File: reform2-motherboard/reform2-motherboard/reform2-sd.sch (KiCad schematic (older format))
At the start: 4 parts, among them J3 SD_Card

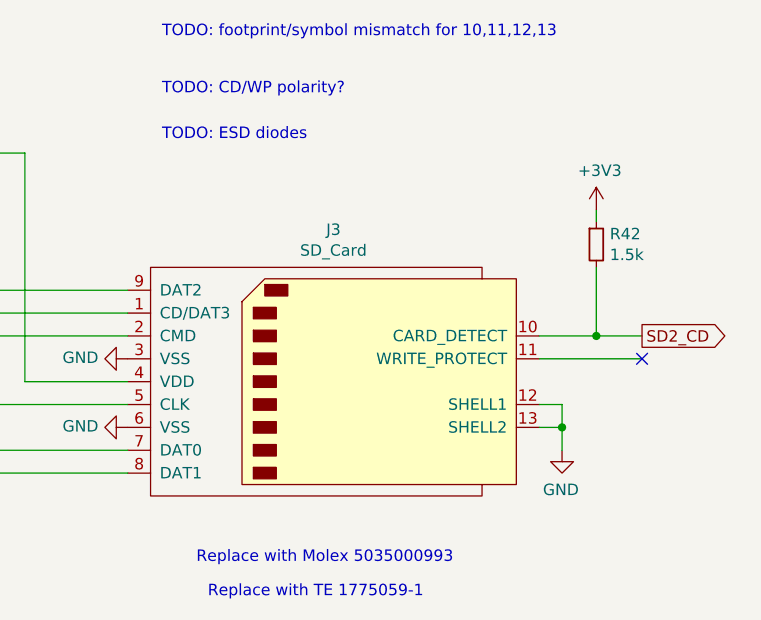
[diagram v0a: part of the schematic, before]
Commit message: reform2 motherboard: pinout and footprint checks completed; ERC checks fixed 100%
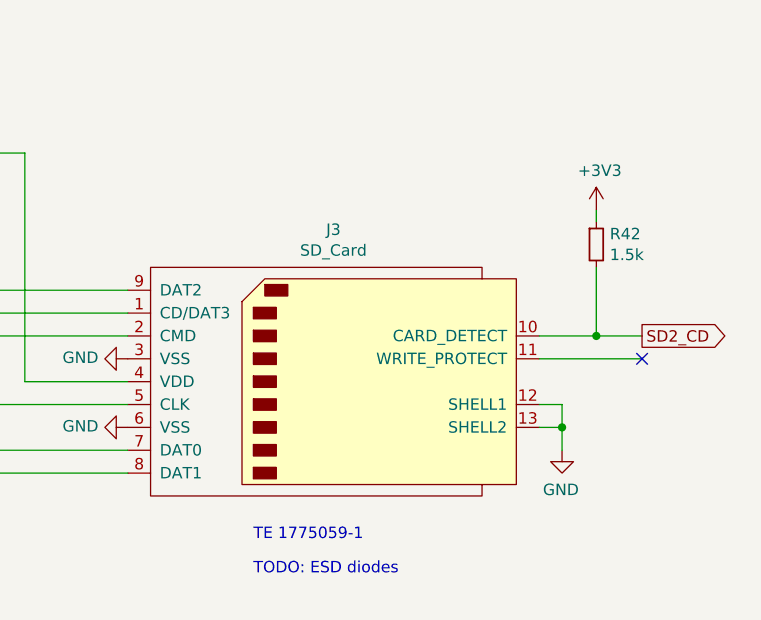
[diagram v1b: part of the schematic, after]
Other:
- note added: "TE 1775059-1"
- note removed: "Replace with Molex 5035000993"
- note removed: "Replace with TE 1775059-1"
- note removed: "TODO: CD/WP polarity?"
- note removed: "TODO: footprint/symbol mismatch for 10,11,12,13"
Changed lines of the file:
@@
 F 1 "SD_Card" H 6200 4024 50  0000 C CNN
 F 2 "footprints:TE_1775059-1" H 6200 3450 50  0001 C CNN
-F 3 "http://portal.fciconnect.com/Comergent//fci/drawing/10067847.pdf" H 6200 3450 50  0001 C CNN
+F 3 "https://www.te.com/usa-en/product-1775059-1.html" H 6200 3450 50  0001 C CNN
 F 4 "TE" H 6200 3450 50  0001 C CNN "Manufacturer"
 F 5 "1775059-1" H 6200 3450 50  0001 C CNN "Manufacturer_No"
@@
 	7200 3550 7200 3650
 Connection ~ 7200 3650
-Text Notes 5450 2400 0    50   ~ 0
+Text Notes 5850 4300 0    50   ~ 0
 TODO: ESD diodes
-Text Notes 5450 2200 0    50   ~ 0
-TODO: CD/WP polarity?
-Text Notes 5600 4250 0    50   ~ 0
-Replace with Molex 5035000993
-Text Notes 5650 4400 0    50   ~ 0
-Replace with TE 1775059-1
+Text Notes 5850 4150 0    50   ~ 0
+TE 1775059-1
 $Comp
 L Device:C_Small C137
@@
 	4050 2650 4400 2650
 Connection ~ 4050 2650
-Text Notes 5450 1950 0    50   ~ 0
-TODO: footprint/symbol mismatch for 10,11,12,13
 NoConn ~ 7550 3350
 $EndSCHEMATC

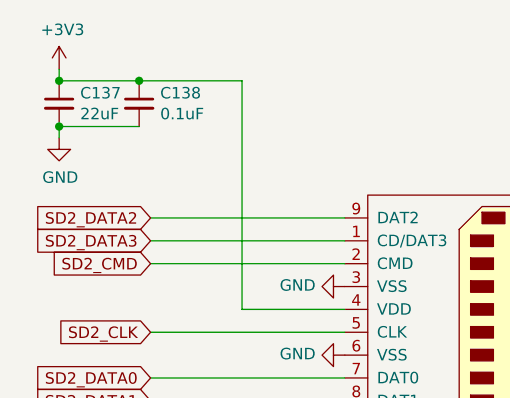
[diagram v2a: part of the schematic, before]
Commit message: reform2 motherboard: add part numbers
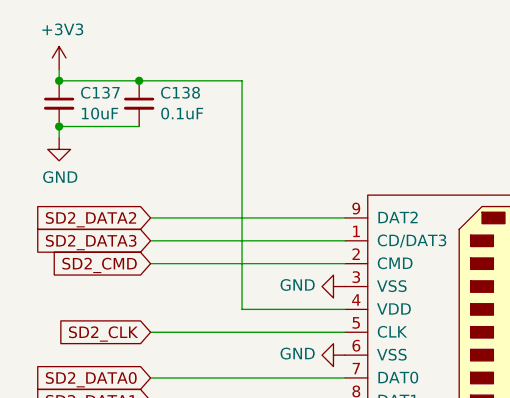
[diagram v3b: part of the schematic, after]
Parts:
- C137: value 22uF -> 10uF
- C138: Manufacturer TDK -> Yageo; Manufacturer_No CGA3E2X8R1E104K080AE -> CC0603JPX7R9BB104
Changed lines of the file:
@@
 P 4050 2550
 F 0 "C137" H 4142 2596 50  0000 L CNN
-F 1 "22uF" H 4142 2505 50  0000 L CNN
+F 1 "10uF" H 4142 2505 50  0000 L CNN
 F 2 "Capacitor_SMD:C_0603_1608Metric" H 4050 2550 50  0001 C CNN
 F 3 "~" H 4050 2550 50  0001 C CNN
@@
 F 2 "Capacitor_SMD:C_0603_1608Metric" H 4400 2550 50  0001 C CNN
 F 3 "~" H 4400 2550 50  0001 C CNN
-F 4 "TDK" H 4400 2550 50  0001 C CNN "Manufacturer"
-F 5 "CGA3E2X8R1E104K080AE" H 4400 2550 50  0001 C CNN "Manufacturer_No"
+F 4 "Yageo" H 4400 2550 50  0001 C CNN "Manufacturer"
+F 5 "CC0603JPX7R9BB104" H 4400 2550 50  0001 C CNN "Manufacturer_No"
 	1    4400 2550
 	1    0    0    -1

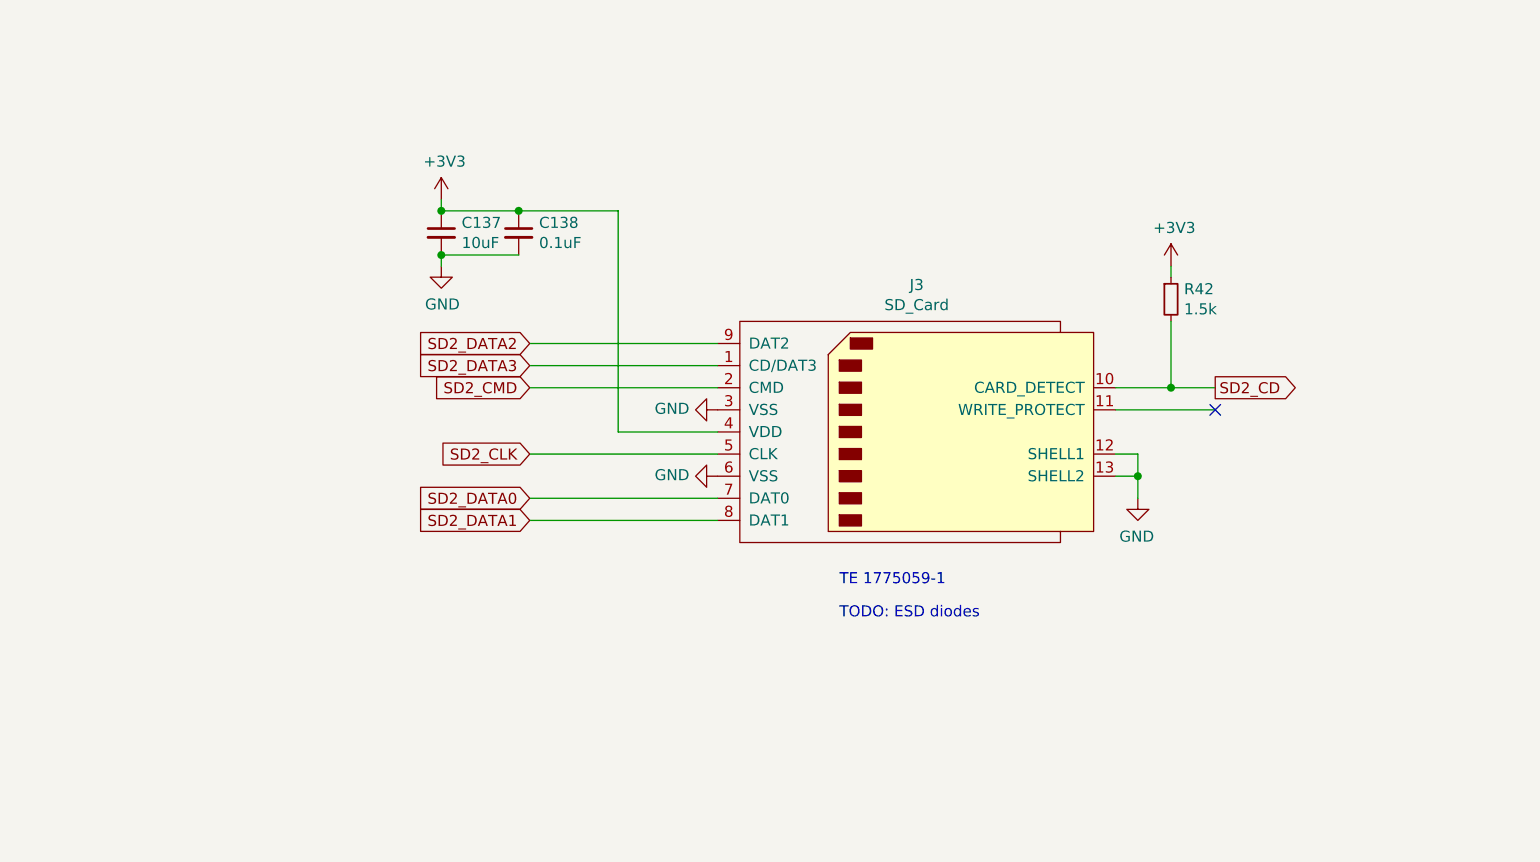
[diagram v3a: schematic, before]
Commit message: Reform 2 Rev 2 WIP: fixed various Rev 1 bugs; consolidate battery connector; consolidate 5v powers; make power rails switchable by LPC; exchange TUSB QFN for TQFP; remove eDP FPC; fixes holes; add SD level shifter; add PCIe clock generator; reduce JTAG footprint
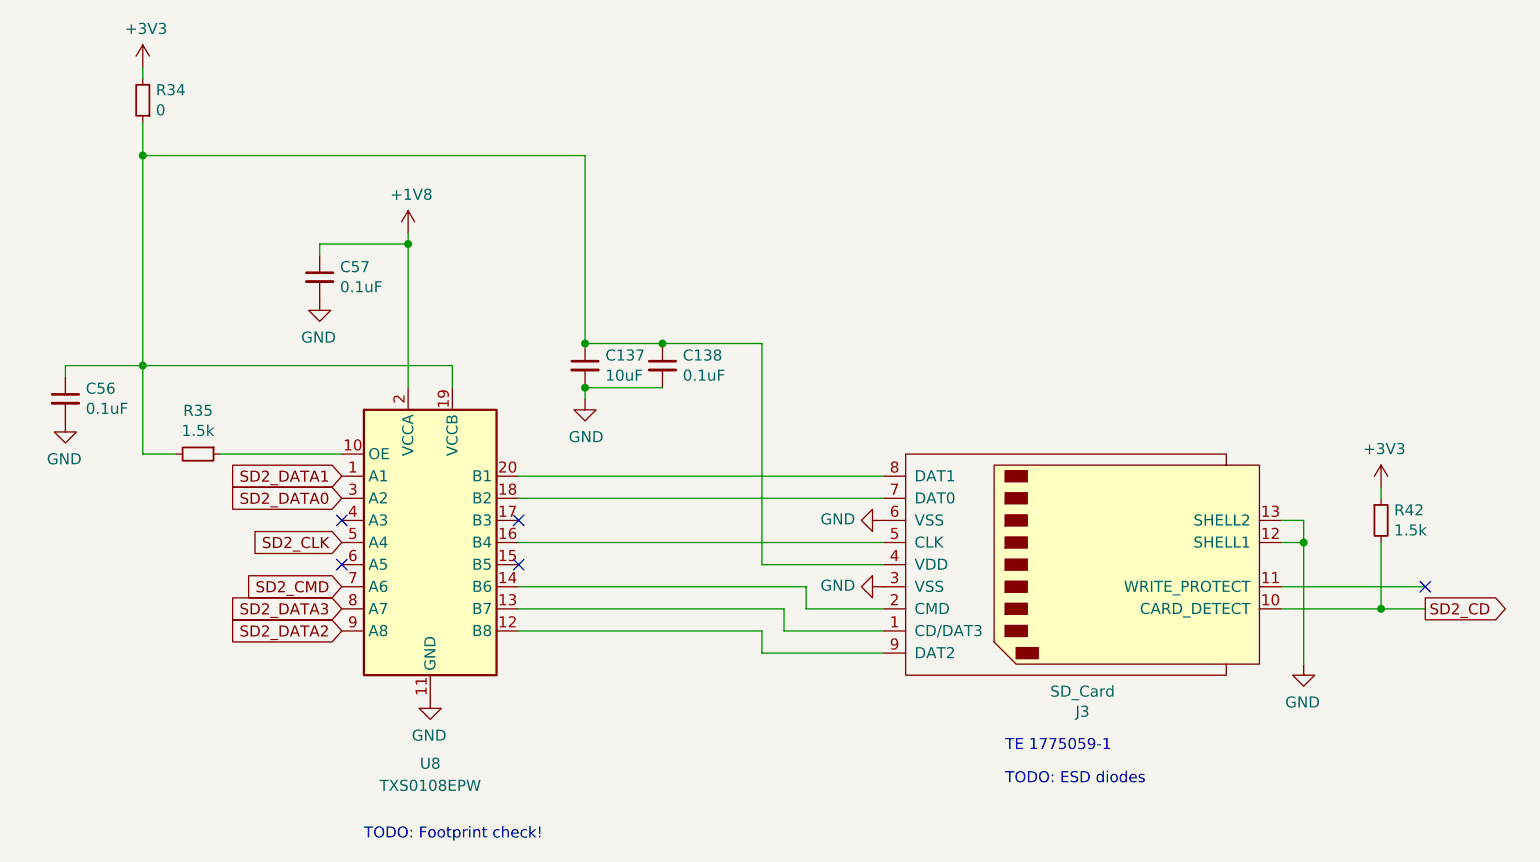
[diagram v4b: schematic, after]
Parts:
- added C56, C57: 0.1uF, Capacitor_SMD:C_0603_1608Metric, symbol Device:C_Small
- added R34: 0, Resistor_SMD:R_0603_1608Metric, symbol Device:R_Small
- added R35: 1.5k, Resistor_SMD:R_0603_1608Metric, symbol Device:R_Small
- added U8: TXS0108EPW, Package_SO:TSSOP-20_4.4x6.5mm_P0.65mm, symbol Logic_LevelTranslator:TXS0108EPW
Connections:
- net +3V3: now also R34.2; no longer C137.1, C138.1, J3.4 (VDD)
- net GND: now also C56.2, C57.2, U8.11 (GND)
- net SD2_CLK: now also U8.5 (A4); no longer J3.5 (CLK)
- net SD2_CMD: now also U8.7 (A6); no longer J3.2 (CMD)
- net SD2_DATA0: now also U8.3 (A2); no longer J3.7 (DAT0)
- net SD2_DATA1: now also U8.1 (A1); no longer J3.8 (DAT1)
- net SD2_DATA2: now also U8.9 (A8); no longer J3.9 (DAT2)
- net SD2_DATA3: now also U8.8 (A7); no longer J3.1 (CD/DAT3)
- new net: J3.1 (CD/DAT3), U8.13 (B7)
- new net: J3.2 (CMD), U8.14 (B6)
- new net: C137.1, C138.1, C56.1, J3.4 (VDD), R34.1, R35.2, U8.19 (VCCB)
- new net: J3.5 (CLK), U8.16 (B4)
- new net: J3.7 (DAT0), U8.18 (B2)
- new net: J3.8 (DAT1), U8.20 (B1)
- new net: J3.9 (DAT2), U8.12 (B8)
- new net: R35.1, U8.10 (OE)
- new net +1V8: C57.1, U8.2 (VCCA)
- no-connect marks 1 -> 5
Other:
- note added: "TODO: Footprint check!"
- moved on the sheet: C137, C138, J3, R42

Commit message: reform2 motherboard: finalize BOM
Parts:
- C137: Manufacturer KEMET -> Murata; Manufacturer_No EDH226M050S9GAA -> GRM188R6YA106MA73D
- R34: Manufacturer (none) -> Vishay Dale; Manufacturer_No (none) -> CRCW06030000Z0EAC
- R35: Manufacturer (none) -> Yageo; Manufacturer_No (none) -> RC0603FR-071K5L
- U8: Manufacturer (none) -> Texas Instruments; Manufacturer_No (none) -> TXS0108EPW
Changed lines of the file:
@@
 F 2 "Capacitor_SMD:C_0603_1608Metric" H 4700 3150 50  0001 C CNN
 F 3 "~" H 4700 3150 50  0001 C CNN
-F 4 "KEMET" H 4700 3150 50  0001 C CNN "Manufacturer"
-F 5 "EDH226M050S9GAA" H 4700 3150 50  0001 C CNN "Manufacturer_No"
+F 4 "Murata" H 4700 3150 50  0001 C CNN "Manufacturer"
+F 5 "GRM188R6YA106MA73D" H 4700 3150 50  0001 C CNN "Manufacturer_No"
 	1    4700 3150
 	1    0    0    -1
@@
 F 2 "Package_SO:TSSOP-20_4.4x6.5mm_P0.65mm" H 4000 3200 50  0001 C CNN
 F 3 "www.ti.com/lit/ds/symlink/txs0108e.pdf" H 4000 3850 50  0001 C CNN
+F 4 "Texas Instruments" H 4000 3950 50  0001 C CNN "Manufacturer"
+F 5 "TXS0108EPW" H 4000 3950 50  0001 C CNN "Manufacturer_No"
 	1    4000 3950
 	1    0    0    -1
@@
 F 2 "Resistor_SMD:R_0603_1608Metric" H 2950 3550 50  0001 C CNN
 F 3 "~" H 2950 3550 50  0001 C CNN
+F 4 "Yageo" H 2950 3550 50  0001 C CNN "Manufacturer"
+F 5 "RC0603FR-071K5L" H 2950 3550 50  0001 C CNN "Manufacturer_No"
 	1    2950 3550
 	0    1    1    0
@@
 F 2 "Resistor_SMD:R_0603_1608Metric" H 2700 1950 50  0001 C CNN
 F 3 "~" H 2700 1950 50  0001 C CNN
+F 4 "Vishay Dale" H 2700 1950 50  0001 C CNN "Manufacturer"
+F 5 "CRCW06030000Z0EAC" H 2700 1950 50  0001 C CNN "Manufacturer_No"
 	1    2700 1950
 	-1   0    0    1

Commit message: WIP reform2 motherboard routing almost complete
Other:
- note added: "TODO: not 1V8?"
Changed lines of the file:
@@
 Text Notes 3700 5300 0    50   ~ 0
 TODO: Footprint check!
+Text Notes 8000 3400 0    50   ~ 0
+TODO: not 1V8?
 $EndSCHEMATC

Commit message: reform2 motherboard: rev2 finished; final checks pending
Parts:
- added R65: 0, Resistor_SMD:R_0603_1608Metric, symbol Device:R_Small
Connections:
- net +1V8: now also R65.2; no longer C57.1, U8.2 (VCCA)
- net +3V3: no longer R42.1
- net at C137.1, C138.1, C56.1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: now also R42.1
- new net: C57.1, R65.1, U8.2 (VCCA)
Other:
- note added: "Includes ESD protection on A port"
- note removed: "TODO: ESD diodes"
- note removed: "TODO: Footprint check!"
- note removed: "TODO: not 1V8?"
- moved on the sheet: C57
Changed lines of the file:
@@
 	8300 4250 7850 4250
-$Comp
-L power:+3V3 #PWR0151
-U 1 1 5D1CBCC0
-P 8300 3700
-F 0 "#PWR0151" H 8300 3550 50  0001 C CNN
-F 1 "+3V3" H 8315 3873 50  0000 C CNN
-F 2 "" H 8300 3700 50  0001 C CNN
-F 3 "" H 8300 3700 50  0001 C CNN
-	1    8300 3700
-	1    0    0    -1
-$EndComp
-Wire Wire Line
-	8300 3700 8300 3750
 $Comp
 L power:GND #PWR0153
@@
 Wire Wire Line
 	7950 3950 7950 3850
-Text Notes 6600 5050 0    50   ~ 0
-TODO: ESD diodes
+Text Notes 3400 5200 0    50   ~ 0
+Includes ESD protection on A port
 Text Notes 6600 4900 0    50   ~ 0
 TE 1775059-1
@@
 L power:+1V8 #PWR0148
 U 1 1 5E92669E
-P 3900 2550
-F 0 "#PWR0148" H 3900 2400 50  0001 C CNN
-F 1 "+1V8" H 3915 2723 50  0000 C CNN
-F 2 "" H 3900 2550 50  0001 C CNN
-F 3 "" H 3900 2550 50  0001 C CNN
-	1    3900 2550
-	1    0    0    -1
-$EndComp
-Wire Wire Line
-	3900 2550 3900 2600
+P 3900 2450
+F 0 "#PWR0148" H 3900 2300 50  0001 C CNN
+F 1 "+1V8" H 3915 2623 50  0000 C CNN
+F 2 "" H 3900 2450 50  0001 C CNN
+F 3 "" H 3900 2450 50  0001 C CNN
+	1    3900 2450
+	1    0    0    -1
+$EndComp
+Wire Wire Line
+	3900 2650 3900 2700
 Wire Wire Line
 	2700 3150 4100 3150
@@
 L Device:C_Small C57
 U 1 1 5E92C316
-P 3500 2750
-F 0 "C57" H 3592 2796 50  0000 L CNN
-F 1 "0.1uF" H 3592 2705 50  0000 L CNN
-F 2 "Capacitor_SMD:C_0603_1608Metric" H 3500 2750 50  0001 C CNN
-F 3 "~" H 3500 2750 50  0001 C CNN
-F 4 "Yageo" H 3500 2750 50  0001 C CNN "Manufacturer"
-F 5 "CC0603JPX7R9BB104" H 3500 2750 50  0001 C CNN "Manufacturer_No"
-	1    3500 2750
+P 3500 2800
+F 0 "C57" H 3592 2846 50  0000 L CNN
+F 1 "0.1uF" H 3592 2755 50  0000 L CNN
+F 2 "Capacitor_SMD:C_0603_1608Metric" H 3500 2800 50  0001 C CNN
+F 3 "~" H 3500 2800 50  0001 C CNN
+F 4 "Yageo" H 3500 2800 50  0001 C CNN "Manufacturer"
+F 5 "CC0603JPX7R9BB104" H 3500 2800 50  0001 C CNN "Manufacturer_No"
+	1    3500 2800
 	1    0    0    -1
 $EndComp
@@
 L power:GND #PWR0150
 U 1 1 5E92E5E4
-P 3500 2850
-F 0 "#PWR0150" H 3500 2600 50  0001 C CNN
-F 1 "GND" H 3505 2677 50  0000 C CNN
-F 2 "" H 3500 2850 50  0001 C CNN
-F 3 "" H 3500 2850 50  0001 C CNN
-	1    3500 2850
+P 3500 2900
+F 0 "#PWR0150" H 3500 2650 50  0001 C CNN
+F 1 "GND" H 3505 2727 50  0000 C CNN
+F 2 "" H 3500 2900 50  0001 C CNN
+F 3 "" H 3500 2900 50  0001 C CNN
+	1    3500 2900
 	-1   0    0    -1
 $EndComp
 Wire Wire Line
-	3900 2600 3500 2600
-Wire Wire Line
-	3500 2600 3500 2650
-Connection ~ 3900 2600
-Wire Wire Line
-	3900 2600 3900 3250
+	3900 2700 3500 2700
+Connection ~ 3900 2700
+Wire Wire Line
+	3900 2700 3900 3250
 $Comp
 L Device:R_Small R34
@@
 	7950 3950 7950 4500
 Connection ~ 7950 3950
-Text Notes 3700 5300 0    50   ~ 0
-TODO: Footprint check!
-Text Notes 8000 3400 0    50   ~ 0
-TODO: not 1V8?
+Wire Wire Line
+	8300 2200 4700 2200
+Wire Wire Line
+	8300 2200 8300 3750
+Connection ~ 4700 2200
+$Comp
+L Device:R_Small R65
+U 1 1 5E039B4B
+P 3900 2550
+F 0 "R65" H 3841 2504 50  0000 R CNN
+F 1 "0" H 3841 2595 50  0000 R CNN
+F 2 "Resistor_SMD:R_0603_1608Metric" H 3900 2550 50  0001 C CNN
+F 3 "~" H 3900 2550 50  0001 C CNN
+F 4 "Vishay Dale" H 3900 2550 50  0001 C CNN "Manufacturer"
+F 5 "CRCW06030000Z0EAC" H 3900 2550 50  0001 C CNN "Manufacturer_No"
+	1    3900 2550
+	-1   0    0    1
+$EndComp
 $EndSCHEMATC

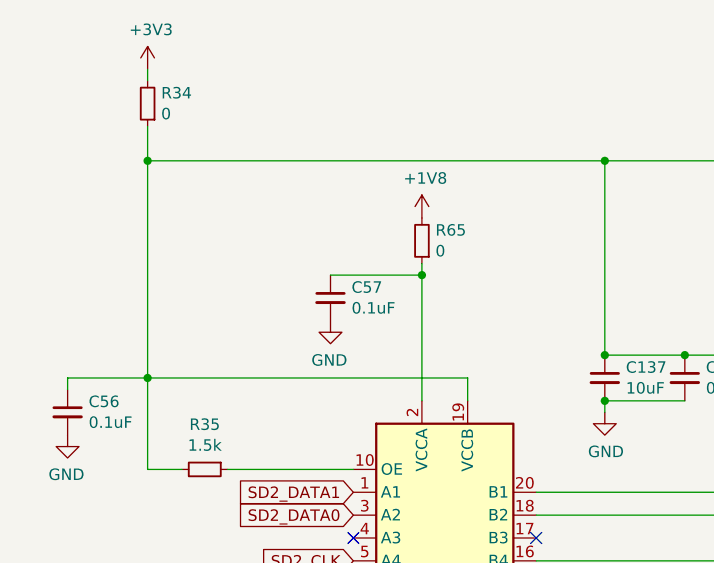
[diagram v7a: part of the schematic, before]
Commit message: Reform 2 motherboard Rev 2 final tweaks before order; added footprints for Molex battery connector and WA SMSI M2 smd screw mounts
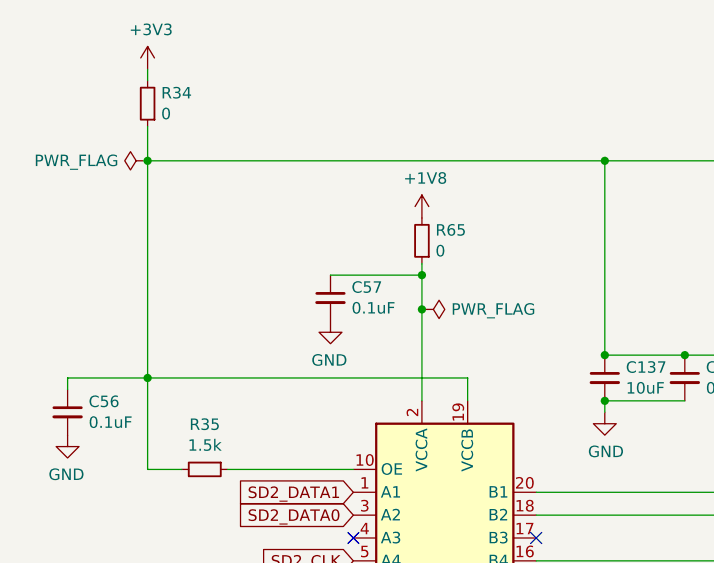
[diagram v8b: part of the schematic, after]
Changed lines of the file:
@@
 Sheet 4 9
 Title "MNT Reform 2 SD Card"
-Date "2019-09-24"
+Date "2019-10-28"
 Rev "2.0D-2"
 Comp "MNT Research GmbH"
@@
 Connection ~ 3900 2700
 Wire Wire Line
-	3900 2700 3900 3250
+	3900 2700 3900 2850
 $Comp
 L Device:R_Small R34
@@
 	-1   0    0    1
 $EndComp
+$Comp
+L power:PWR_FLAG #FLG0117
+U 1 1 5EC4072D
+P 3900 2850
+F 0 "#FLG0117" H 3900 2925 50  0001 C CNN
+F 1 "PWR_FLAG" V 3900 2978 50  0000 L CNN
+F 2 "" H 3900 2850 50  0001 C CNN
+F 3 "~" H 3900 2850 50  0001 C CNN
+	1    3900 2850
+	0    1    1    0
+$EndComp
+Connection ~ 3900 2850
+Wire Wire Line
+	3900 2850 3900 3250
+$Comp
+L power:PWR_FLAG #FLG0118
+U 1 1 5EC40BBD
+P 2700 2200
+F 0 "#FLG0118" H 2700 2275 50  0001 C CNN
+F 1 "PWR_FLAG" V 2700 2327 50  0000 L CNN
+F 2 "" H 2700 2200 50  0001 C CNN
+F 3 "~" H 2700 2200 50  0001 C CNN
+	1    2700 2200
+	0    -1   -1   0
+$EndComp
 $EndSCHEMATC
